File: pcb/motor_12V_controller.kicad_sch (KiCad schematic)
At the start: 39 parts, among them IC1 RP2040-ZERO, J1 01x02, J2 01x02, U1 AP63200WU, U2 L293D

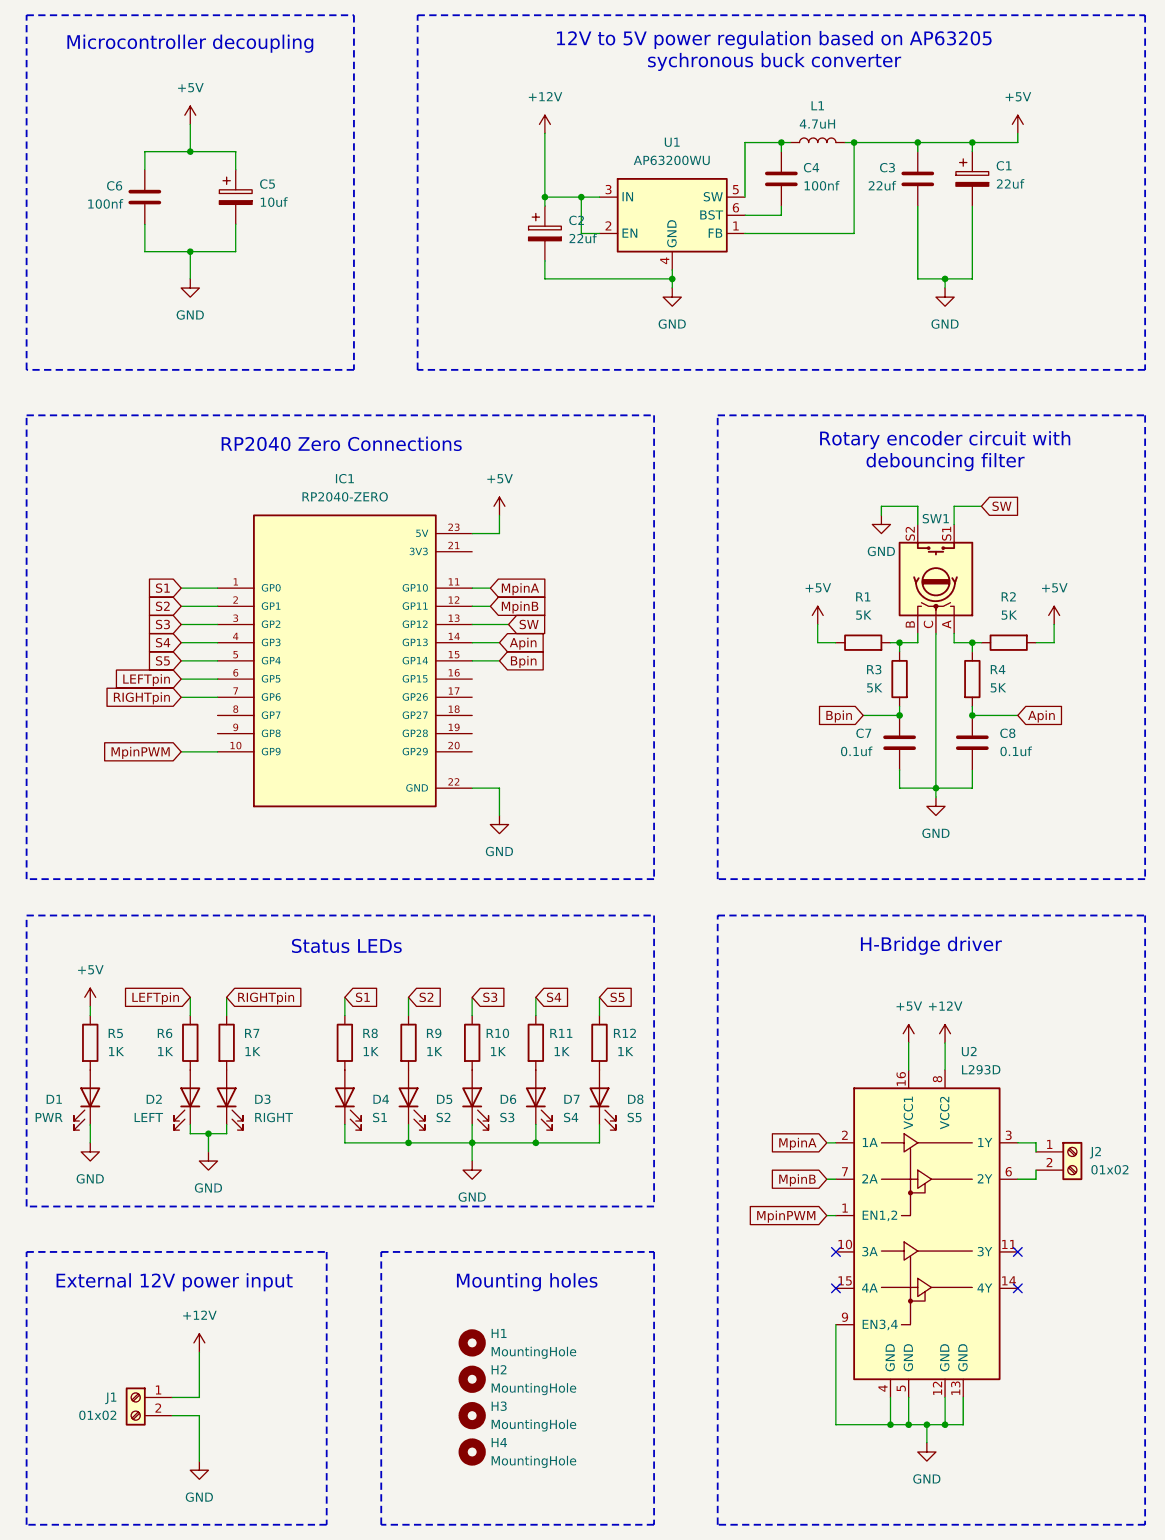
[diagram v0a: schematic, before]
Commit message: Swapped the connections to to create more compact PCB design.
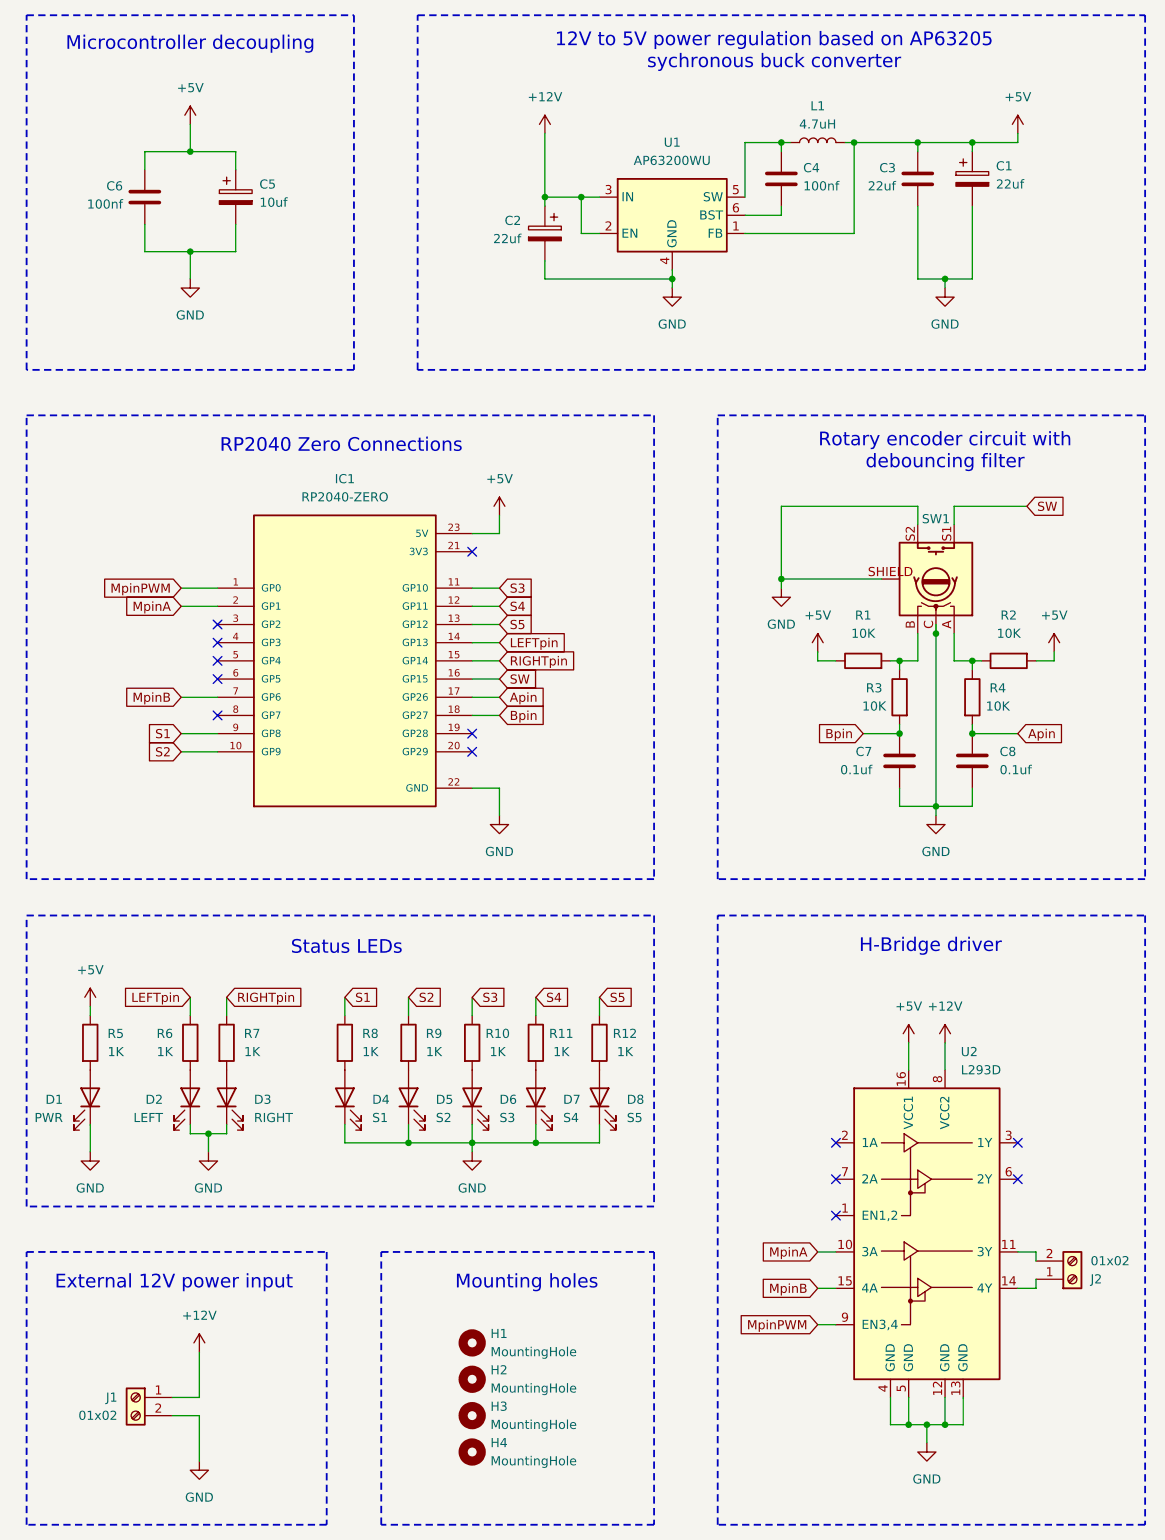
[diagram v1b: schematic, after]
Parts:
- C1, C2, C5: footprint (none) -> Capacitor_SMD:C_1210_3225Metric_Pad1.33x2.70mm_HandSolder
- C3, C4, C6: footprint (none) -> Capacitor_SMD:C_0402_1005Metric
- C7, C8: footprint (none) -> Capacitor_SMD:C_0201_0603Metric
- D1, D2, D3, D4, D5, D6, D7, D8: footprint (none) -> LED_SMD:LED_0201_0603Metric
- J1, J2: footprint (none) -> TerminalBlock:TerminalBlock_Xinya_XY308-2.54-2P_1x02_P2.54mm_Horizontal
- L1: footprint (none) -> Inductor_SMD:L_1008_2520Metric_Pad1.43x2.20mm_HandSolder
- R1, R2, R3, R4: value 5K -> 10K; footprint (none) -> Resistor_SMD:R_1206_3216Metric_Pad1.30x1.75mm_HandSolder
- R10, R11, R12, R6, R7, R8, R9: footprint (none) -> Resistor_SMD:R_0201_0603Metric
- R5: footprint (none) -> Resistor_SMD:R_1206_3216Metric
- SW1: footprint (none) -> PEC11R-4215F-S0024:XDCR_PEC11R-4215F-S0024
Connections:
- net Apin: now also IC1.17 (GP26); no longer IC1.14 (GP13)
- net Bpin: now also IC1.18 (GP27); no longer IC1.15 (GP14)
- net GND: now also SW1.SHIELD; no longer U2.9 (EN3,4)
- net LEFTpin: now also IC1.14 (GP13); no longer IC1.6 (GP5)
- net MpinA: now also IC1.2 (GP1), U2.10 (3A); no longer IC1.11 (GP10), U2.2 (1A)
- net MpinB: now also IC1.7 (GP6), U2.15 (4A); no longer IC1.12 (GP11), U2.7 (2A)
- net MpinPWM: now also IC1.1 (GP0), U2.9 (EN3,4); no longer IC1.10 (GP9), U2.1 (EN1,2)
- net RIGHTpin: now also IC1.15 (GP14); no longer IC1.7 (GP6)
- net S1: now also IC1.9 (GP8); no longer IC1.1 (GP0)
- net S2: now also IC1.10 (GP9); no longer IC1.2 (GP1)
- net S3: now also IC1.11 (GP10); no longer IC1.3 (GP2)
- net S4: now also IC1.12 (GP11); no longer IC1.4 (GP3)
- net S5: now also IC1.13 (GP12); no longer IC1.5 (GP4)
- net SW: now also IC1.16 (GP15); no longer IC1.13 (GP12)
- net at U2.11 (3Y): now also J2.2 (Pin_2)
- net at U2.14 (4Y): now also J2.1 (Pin_1)
- net at U2.3 (1Y): no longer J2.1 (Pin_1)
- net at U2.6 (2Y): no longer J2.2 (Pin_2)
- no-connect marks 4 -> 13
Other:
- moved on the sheet: C7, C8, J2, R1, R2, R3, R4

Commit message: Changed the rotary encoder's circuit part to use 3.3V voltage logic, since it is connected toRP2040 pins.
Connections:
- net +5V: no longer R1.1, R2.2
- net +3.3V: now reaches IC1.21 (3V3)
- net +3.3V: now also R1.1, R2.2
- no-connect marks 13 -> 12
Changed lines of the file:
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@@
 	)
 	(no_connect
-		(at 92.71 105.41)
-	)
-	(no_connect
 		(at 57.15 123.19)
 	)
@@
 	(wire
 		(pts
+			(xy 92.71 105.41) (xy 101.6 105.41)
+		)
+		(stroke
+			(width 0)
+			(type default)
+		)
+	)
+	(wire
+		(pts
 			(xy 101.6 185.42) (xy 101.6 187.96)
 		)
@@
 	(wire
 		(pts
+			(xy 101.6 105.41) (xy 101.6 100.33)
+		)
+		(stroke
+			(width 0)
+			(type default)
+		)
+	)
+	(wire
+		(pts
 			(xy 58.42 185.42) (xy 58.42 186.69)
 		)
@@
 	)
 	(symbol
+		(lib_id "power:+3.3V")
+		(at 173.99 119.38 0)
+		(unit 1)
+		(exclude_from_sim no)
+		(in_bom yes)
+		(on_board yes)
+		(dnp no)
+		(fields_autoplaced yes)
+		(property "Reference" "#PWR09"
+			(at 173.99 123.19 0)
+			(effects
+				(font
+					(size 1.27 1.27)
+				)
+				(hide yes)
+			)
+		)
+		(property "Value" "+3.3V"
+			(at 173.99 114.3 0)
+			(effects
+				(font
+					(size 1.27 1.27)
+				)
+			)
+		)
+		(property "Footprint" ""
+			(at 173.99 119.38 0)
+			(effects
+				(font
+					(size 1.27 1.27)
+				)
+				(hide yes)
+			)
+		)
+		(property "Datasheet" ""
+			(at 173.99 119.38 0)
+			(effects
+				(font
+					(size 1.27 1.27)
+				)
+				(hide yes)
+			)
+		)
+		(property "Description" "Power symbol creates a global label with name \"+3.3V\""
+			(at 173.99 119.38 0)
+			(effects
+				(font
+					(size 1.27 1.27)
+				)
+				(hide yes)
+			)
+		)
+		(pin "1"
+		)
+		(instances
+			(project "motor_12V_controller"
+				(path "/a052a212-daee-4b53-b871-fe44b9361b51"
+					(reference "#PWR09")
+					(unit 1)
+				)
+			)
+		)
+	)
+	(symbol
 		(lib_id "Device:R")
 		(at 74.93 173.99 0)
@@
 	)
 	(symbol
+		(lib_id "power:+3.3V")
+		(at 101.6 100.33 0)
+		(unit 1)
+		(exclude_from_sim no)
+		(in_bom yes)
+		(on_board yes)
+		(dnp no)
+		(fields_autoplaced yes)
+		(property "Reference" "#PWR022"
+			(at 101.6 104.14 0)
+			(effects
+				(font
+					(size 1.27 1.27)
+				)
+				(hide yes)
+			)
+		)
+		(property "Value" "+3.3V"
+			(at 101.6 95.25 0)
+			(effects
+				(font
+					(size 1.27 1.27)
+				)
+			)
+		)
+		(property "Footprint" ""
+			(at 101.6 100.33 0)
+			(effects
+				(font
+					(size 1.27 1.27)
+				)
+				(hide yes)
+			)
+		)
+		(property "Datasheet" ""
+			(at 101.6 100.33 0)
+			(effects
+				(font
+					(size 1.27 1.27)
+				)
+				(hide yes)
+			)
+		)
+		(property "Description" "Power symbol creates a global label with name \"+3.3V\""
+			(at 101.6 100.33 0)
+			(effects
+				(font
+					(size 1.27 1.27)
+				)
+				(hide yes)
+			)
+		)
+		(pin "1"
+		)
+		(instances
+			(project "motor_12V_controller"
+				(path "/a052a212-daee-4b53-b871-fe44b9361b51"
+					(reference "#PWR022")
+					(unit 1)
+				)
+			)
+		)
+	)
+	(symbol
 		(lib_id "Device:R")
 		(at 53.34 173.99 0)
@@
 	)
 	(symbol
-		(lib_id "power:+5V")
+		(lib_id "power:+3.3V")
 		(at 140.97 119.38 0)
 		(unit 1)
@@
 			)
 		)
-		(property "Value" "+5V"
+		(property "Value" "+3.3V"
 			(at 140.97 114.3 0)
 			(effects
@@
 			)
 		)
-		(property "Description" "Power symbol creates a global label with name \"+5V\""
+		(property "Description" "Power symbol creates a global label with name \"+3.3V\""
 			(at 140.97 119.38 0)
 			(effects
@@
 		)
 		(instances
-			(project "motor_14V_controller"
+			(project ""
 				(path "/a052a212-daee-4b53-b871-fe44b9361b51"
 					(reference "#PWR08")
@@
 					(unit 1)
 				)
-			)
-		)
-	)
-	(symbol
-		(lib_id "power:+5V")
-		(at 173.99 119.38 0)
-		(unit 1)
-		(exclude_from_sim no)
-		(in_bom yes)
-		(on_board yes)
-		(dnp no)
-		(fields_autoplaced yes)
-		(property "Reference" "#PWR09"
-			(at 173.99 123.19 0)
-			(effects
-				(font
-					(size 1.27 1.27)
-				)
-				(hide yes)
-			)
-		)
-		(property "Value" "+5V"
-			(at 173.99 114.3 0)
-			(effects
-				(font
-					(size 1.27 1.27)
-				)
-			)
-		)
-		(property "Footprint" ""
-			(at 173.99 119.38 0)
-			(effects
-				(font
-					(size 1.27 1.27)
-				)
-				(hide yes)
-			)
-		)
-		(property "Datasheet" ""
-			(at 173.99 119.38 0)
-			(effects
-				(font
-					(size 1.27 1.27)
-				)
-				(hide yes)
-			)
-		)
-		(property "Description" "Power symbol creates a global label with name \"+5V\""
-			(at 173.99 119.38 0)
-			(effects
-				(font
-					(size 1.27 1.27)
-				)
-				(hide yes)
-			)
-		)
-		(pin "1"
-		)
-		(instances
-			(project "motor_14V_controller"
-				(path "/a052a212-daee-4b53-b871-fe44b9361b51"
-					(reference "#PWR09")
-					(unit 1)
-				)

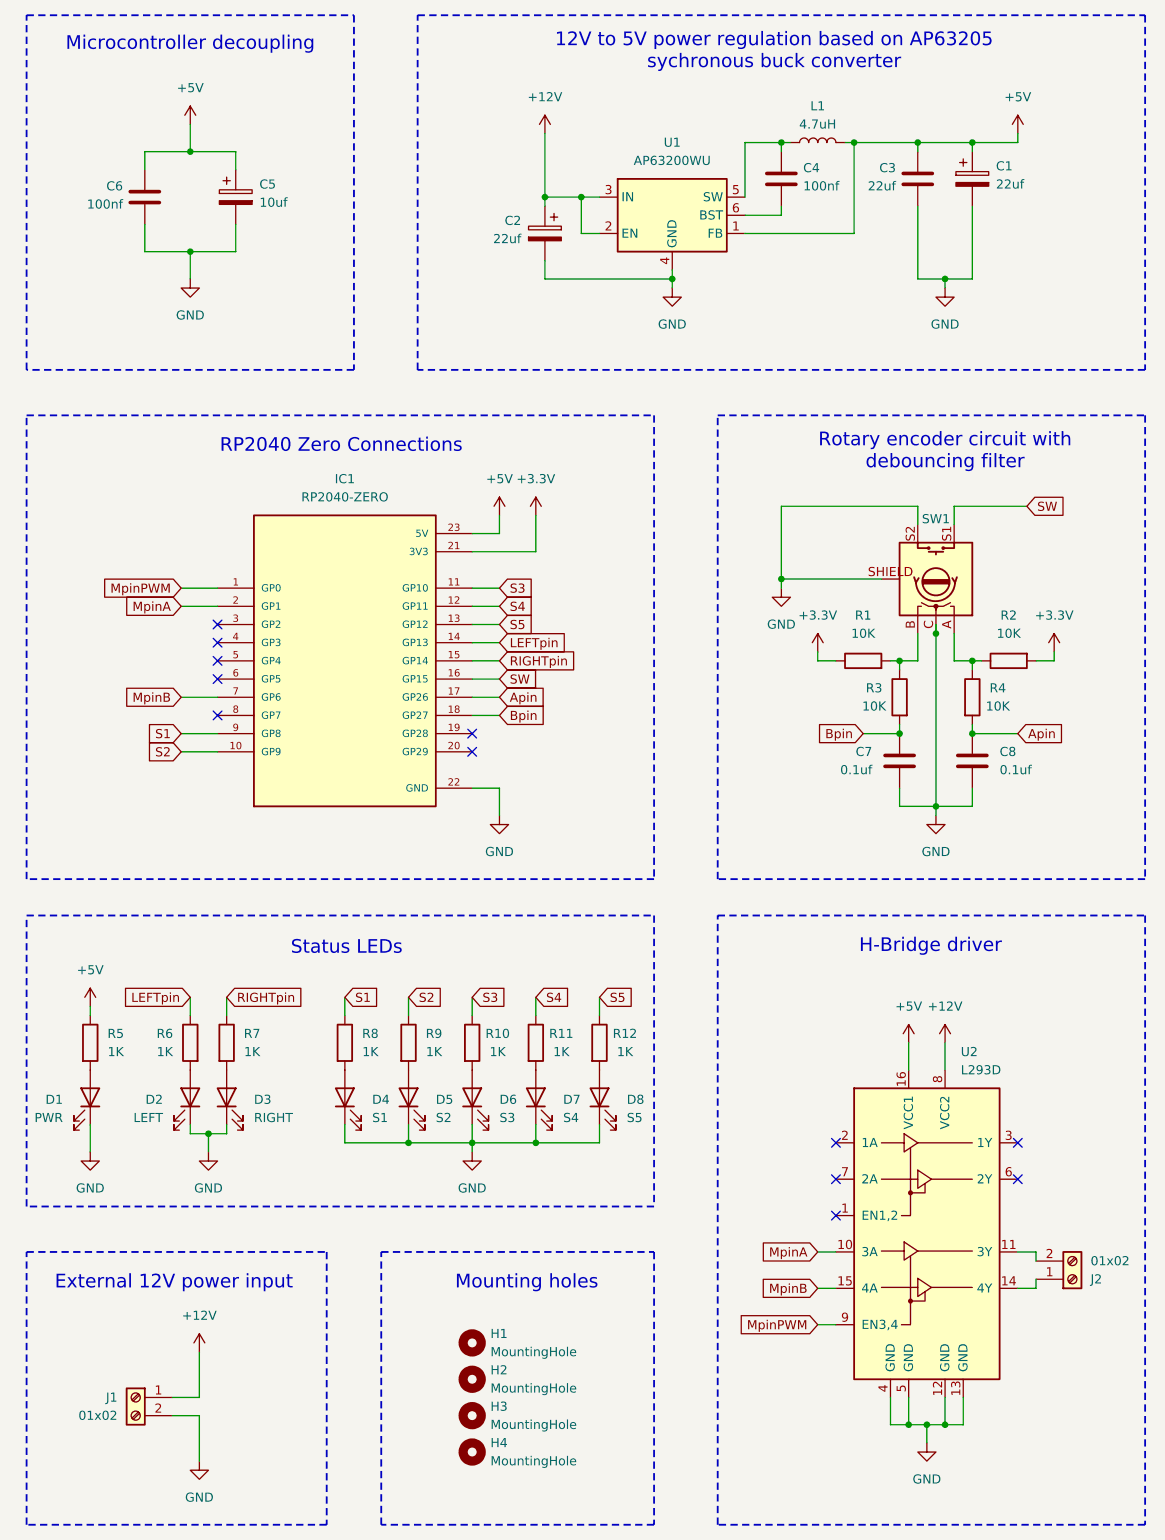
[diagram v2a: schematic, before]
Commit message: Updated the schematic for better match of footprints for tht elements.
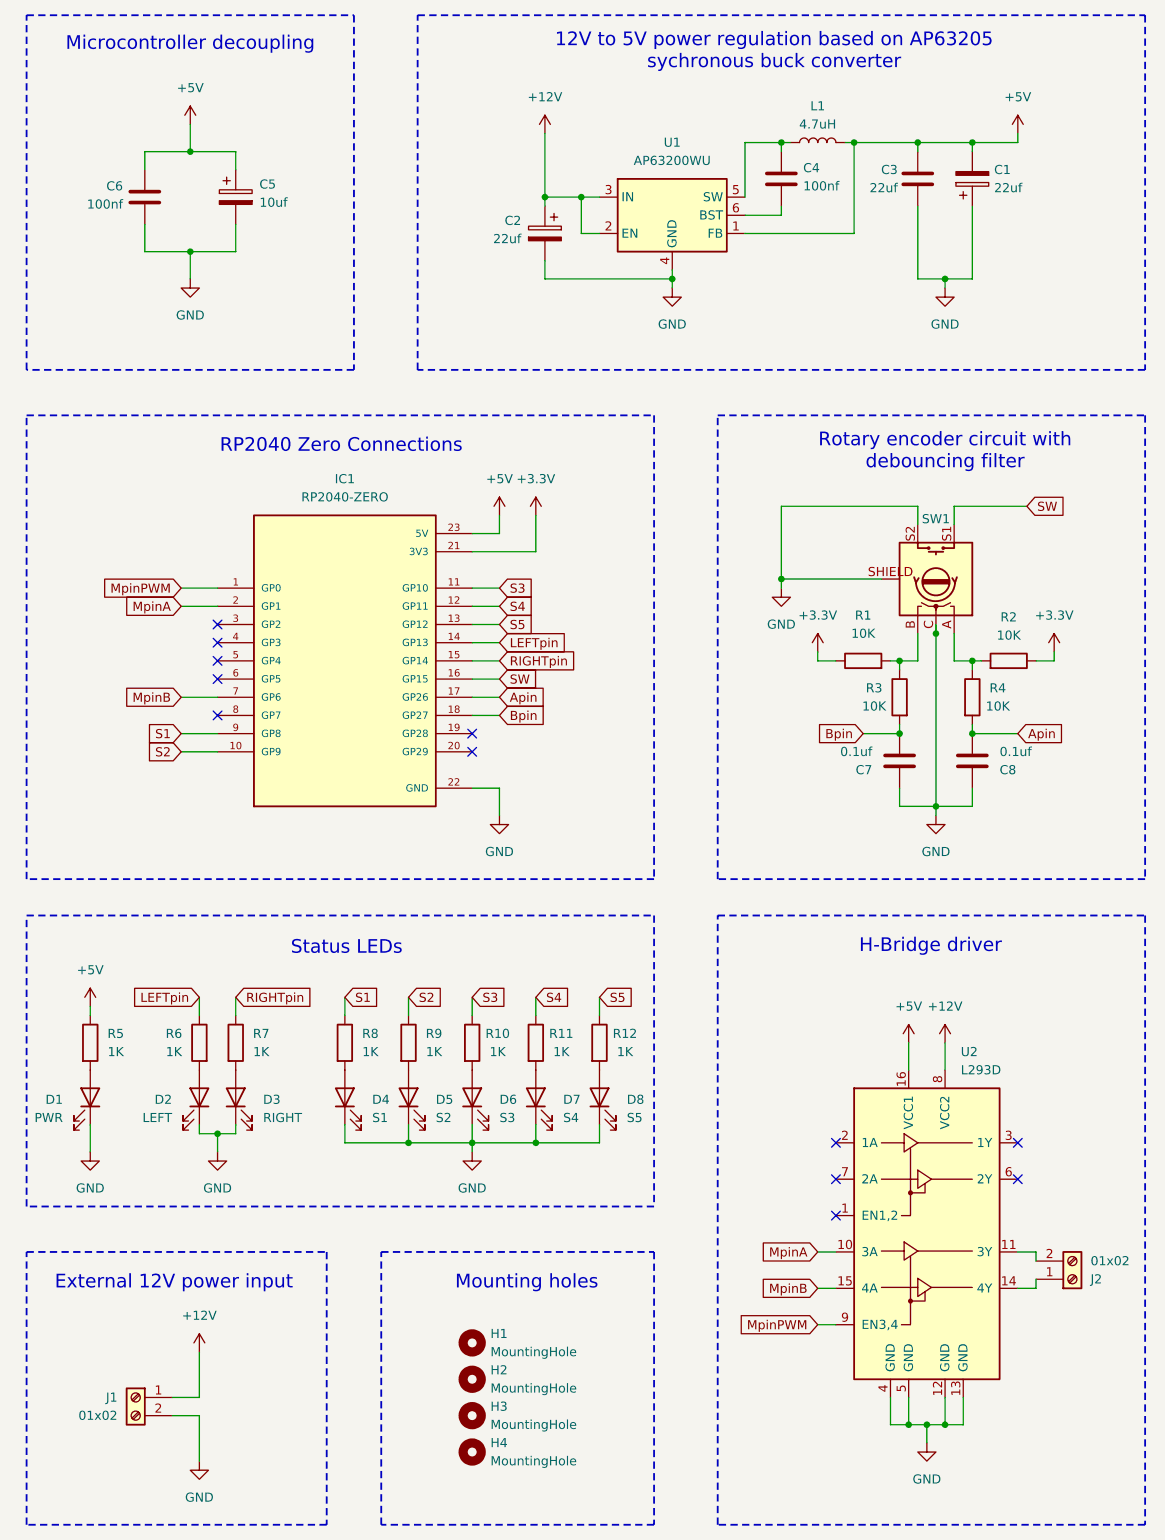
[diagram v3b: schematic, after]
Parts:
- C1, C2, C5: footprint Capacitor_SMD:C_1210_3225Metric_Pad1.33x2.70mm_HandSolder -> Capacitor_THT:CP_Radial_D4.0mm_P1.50mm
- C3, C4, C6: footprint Capacitor_SMD:C_0402_1005Metric -> Capacitor_THT:CP_Radial_D4.0mm_P1.50mm
- C7, C8: footprint Capacitor_SMD:C_0201_0603Metric -> Capacitor_THT:CP_Radial_D4.0mm_P1.50mm
- D1, D2, D3, D4, D5, D6, D7, D8: footprint LED_SMD:LED_0201_0603Metric -> LED_THT:LED_Rectangular_W5.0mm_H2.0mm
- L1: footprint Inductor_SMD:L_1008_2520Metric_Pad1.43x2.20mm_HandSolder -> Inductor_THT:L_Radial_L7.5mm_W4.6mm_P5.00mm_Neosid_SD75
- R1, R2, R3, R4: footprint Resistor_SMD:R_1206_3216Metric_Pad1.30x1.75mm_HandSolder -> Resistor_THT:R_Axial_DIN0204_L3.6mm_D1.6mm_P2.54mm_Vertical
- R10, R11, R12, R6, R7, R8, R9: footprint Resistor_SMD:R_0201_0603Metric -> Resistor_THT:R_Axial_DIN0204_L3.6mm_D1.6mm_P2.54mm_Vertical
- R5: footprint Resistor_SMD:R_1206_3216Metric -> Resistor_THT:R_Axial_DIN0204_L3.6mm_D1.6mm_P2.54mm_Vertical
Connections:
- net +3.3V: now also R2.1; no longer R2.2
- net +5V: now also C1.2, C3.2, C6.1; no longer C1.1, C3.1, C6.2
- net Apin: now also C8.2; no longer C8.1
- net Bpin: now also C7.2; no longer C7.1
- net GND: now also C1.1, C3.1, C6.2, C7.1, C8.1; no longer C1.2, C3.2, C6.1, C7.2, C8.2
- net at R4.1, SW1.A: now also R2.2; no longer R2.1
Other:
- moved on the sheet: C3, C6, C7, D2, D3, R2, R6, R7
